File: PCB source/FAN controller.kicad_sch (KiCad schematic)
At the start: 9 parts, among them M1 Fan, Q1 AO3400A

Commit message: Do Cleanup
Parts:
- renumbered C40 to C49, C22 to C50, D1 to D4, Q1 to Q4, R10 to R23, R11 to R24, R13 to R25, R12 to R26
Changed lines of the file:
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@@
 		(dnp no)
 		(fields_autoplaced yes)
-		(property "Reference" "#PWR039"
+		(property "Reference" "#PWR099"
 			(at 100.33 78.74 0)
 			(effects
@@
 			(project ""
 				(path "/3103c9de-f1ba-4d51-8bfc-798df1c75e2f/ddd125ab-d3f0-4627-8bf0-c5c0a9168cb7"
-					(reference "#PWR039")
+					(reference "#PWR099")
 					(unit 1)
 				)
@@
 		(on_board yes)
 		(dnp yes)
-		(property "Reference" "R10"
+		(property "Reference" "R23"
 			(at 114.554 78.486 90)
 			(effects
@@
 			(project ""
 				(path "/3103c9de-f1ba-4d51-8bfc-798df1c75e2f/ddd125ab-d3f0-4627-8bf0-c5c0a9168cb7"
-					(reference "R10")
+					(reference "R23")
 					(unit 1)
 				)
@@
 		(dnp no)
 		(fields_autoplaced yes)
-		(property "Reference" "#PWR038"
+		(property "Reference" "#PWR0100"
 			(at 109.22 78.74 0)
 			(effects
@@
 			(project ""
 				(path "/3103c9de-f1ba-4d51-8bfc-798df1c75e2f/ddd125ab-d3f0-4627-8bf0-c5c0a9168cb7"
-					(reference "#PWR038")
+					(reference "#PWR0100")
 					(unit 1)
 				)
@@
 		(dnp no)
 		(fields_autoplaced yes)
-		(property "Reference" "Q1"
+		(property "Reference" "Q4"
 			(at 175.26 114.3 0)
 			(effects
@@
 			(project ""
 				(path "/3103c9de-f1ba-4d51-8bfc-798df1c75e2f/ddd125ab-d3f0-4627-8bf0-c5c0a9168cb7"
-					(reference "Q1")
+					(reference "Q4")
 					(unit 1)
 				)
@@
 		(dnp no)
 		(fields_autoplaced yes)
-		(property "Reference" "#PWR041"
+		(property "Reference" "#PWR0102"
 			(at 152.4 135.89 0)
 			(effects
@@
 			(project "OrangePie"
 				(path "/3103c9de-f1ba-4d51-8bfc-798df1c75e2f/ddd125ab-d3f0-4627-8bf0-c5c0a9168cb7"
-					(reference "#PWR041")
+					(reference "#PWR0102")
 					(unit 1)
 				)
@@
 		(dnp no)
 		(fields_autoplaced yes)
-		(property "Reference" "R13"
+		(property "Reference" "R25"
 			(at 142.24 111.76 90)
 			(effects
@@
 			(project ""
 				(path "/3103c9de-f1ba-4d51-8bfc-798df1c75e2f/ddd125ab-d3f0-4627-8bf0-c5c0a9168cb7"
-					(reference "R13")
+					(reference "R25")
 					(unit 1)
 				)
@@
 		(dnp no)
 		(fields_autoplaced yes)
-		(property "Reference" "C40"
+		(property "Reference" "C49"
 			(at 157.48 93.98 0)
 			(effects
@@
 			(project "OrangePie"
 				(path "/3103c9de-f1ba-4d51-8bfc-798df1c75e2f/ddd125ab-d3f0-4627-8bf0-c5c0a9168cb7"
-					(reference "C40")
+					(reference "C49")
 					(unit 1)
 				)
@@
 		(dnp no)
 		(fields_autoplaced yes)
-		(property "Reference" "R12"
+		(property "Reference" "R26"
 			(at 154.94 121.92 0)
 			(effects
@@
 			(project ""
 				(path "/3103c9de-f1ba-4d51-8bfc-798df1c75e2f/ddd125ab-d3f0-4627-8bf0-c5c0a9168cb7"
-					(reference "R12")
+					(reference "R26")
 					(unit 1)
 				)
@@
 		(on_board yes)
 		(dnp no)
-		(property "Reference" "C22"
+		(property "Reference" "C50"
 			(at 148.844 96.52 90)
 			(effects
@@
 			(project "OrangePie"
 				(path "/3103c9de-f1ba-4d51-8bfc-798df1c75e2f/ddd125ab-d3f0-4627-8bf0-c5c0a9168cb7"
-					(reference "C22")
+					(reference "C50")
 					(unit 1)
 				)
@@
 		(dnp no)
 		(fields_autoplaced yes)
-		(property "Reference" "D1"
+		(property "Reference" "D4"
 			(at 187.96 94.615 0)
 			(effects
@@
 			(project ""
 				(path "/3103c9de-f1ba-4d51-8bfc-798df1c75e2f/ddd125ab-d3f0-4627-8bf0-c5c0a9168cb7"
-					(reference "D1")
+					(reference "D4")
 					(unit 1)
 				)
@@
 		(dnp no)
 		(fields_autoplaced yes)
-		(property "Reference" "#PWR043"
+		(property "Reference" "#PWR0103"
 			(at 171.45 135.89 0)
 			(effects
@@
 			(project "OrangePie"
 				(path "/3103c9de-f1ba-4d51-8bfc-798df1c75e2f/ddd125ab-d3f0-4627-8bf0-c5c0a9168cb7"
-					(reference "#PWR043")
+					(reference "#PWR0103")
 					(unit 1)
 				)
@@
 		(on_board yes)
 		(dnp no)
-		(property "Reference" "#PWR042"
+		(property "Reference" "#PWR0101"
 			(at 154.94 111.76 0)
 			(effects
@@
 			(project "OrangePie"
 				(path "/3103c9de-f1ba-4d51-8bfc-798df1c75e2f/ddd125ab-d3f0-4627-8bf0-c5c0a9168cb7"
-					(reference "#PWR042")
+					(reference "#PWR0101")
 					(unit 1)
 				)
@@
 		(on_board yes)
 		(dnp no)
-		(property "Reference" "R11"
+		(property "Reference" "R24"
 			(at 114.3 87.122 90)
 			(effects
@@
 			(project "OrangePie"
 				(path "/3103c9de-f1ba-4d51-8bfc-798df1c75e2f/ddd125ab-d3f0-4627-8bf0-c5c0a9168cb7"
-					(reference "R11")
+					(reference "R24")
 					(unit 1)
 				)

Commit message: Pass ERC
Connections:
- net +12V renamed 12V_IN
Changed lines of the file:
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@@
 	(wire
 		(pts
-			(xy 100.33 74.93) (xy 100.33 88.9)
+			(xy 87.63 86.36) (xy 87.63 88.9)
 		)
 		(stroke
@@
 	(wire
 		(pts
+			(xy 102.87 80.01) (xy 115.57 80.01)
+		)
+		(stroke
+			(width 0)
+			(type default)
+		)
+	)
+	(wire
+		(pts
 			(xy 133.35 83.82) (xy 133.35 88.9)
 		)
@@
 	(wire
 		(pts
-			(xy 109.22 80.01) (xy 115.57 80.01)
-		)
-		(stroke
-			(width 0)
-			(type default)
-		)
-	)
-	(wire
-		(pts
 			(xy 154.94 88.9) (xy 148.59 88.9)
 		)
@@
 	(wire
 		(pts
-			(xy 109.22 74.93) (xy 109.22 80.01)
-		)
-		(stroke
-			(width 0)
-			(type default)
-		)
-	)
-	(wire
-		(pts
 			(xy 185.42 83.82) (xy 171.45 83.82)
 		)
@@
 	(wire
 		(pts
-			(xy 100.33 88.9) (xy 115.57 88.9)
+			(xy 87.63 88.9) (xy 115.57 88.9)
 		)
 		(stroke
@@
 			(width 0)
 			(type default)
+		)
+	)
+	(hierarchical_label "12V_IN"
+		(shape input)
+		(at 102.87 80.01 180)
+		(fields_autoplaced yes)
+		(effects
+			(font
+				(size 1.27 1.27)
+			)
+			(justify right)
 		)
 	)
@@
 	(symbol
 		(lib_id "power:+5V")
-		(at 100.33 74.93 0)
+		(at 87.63 86.36 0)
 		(unit 1)
 		(exclude_from_sim no)
@@
 		(fields_autoplaced yes)
 		(property "Reference" "#PWR099"
-			(at 100.33 78.74 0)
+			(at 87.63 90.17 0)
 			(effects
 				(font
@@
 		)
 		(property "Value" "+5V"
-			(at 100.33 69.85 0)
+			(at 87.63 81.28 0)
 			(effects
 				(font
@@
 		)
 		(property "Footprint" ""
-			(at 100.33 74.93 0)
+			(at 87.63 86.36 0)
 			(effects
 				(font
@@
 		)
 		(property "Datasheet" ""
-			(at 100.33 74.93 0)
+			(at 87.63 86.36 0)
 			(effects
 				(font
@@
 		)
 		(property "Description" "Power symbol creates a global label with name \"+5V\""
-			(at 100.33 74.93 0)
+			(at 87.63 86.36 0)
 			(effects
 				(font
@@
 					(unit 1)
 				)
-			)
-		)
-	)
-	(symbol
-		(lib_id "power:+12V")
-		(at 109.22 74.93 0)
-		(unit 1)
-		(exclude_from_sim no)
-		(in_bom yes)
-		(on_board yes)
-		(dnp no)
-		(fields_autoplaced yes)
-		(property "Reference" "#PWR0100"
-			(at 109.22 78.74 0)
-			(effects
-				(font
-					(size 1.27 1.27)
-				)
-				(hide yes)
-			)
-		)
-		(property "Value" "+12V"
-			(at 109.22 69.85 0)
-			(effects
-				(font
-					(size 1.27 1.27)
-				)
-			)
-		)
-		(property "Footprint" ""
-			(at 109.22 74.93 0)
-			(effects
-				(font
-					(size 1.27 1.27)
-				)
-				(hide yes)
-			)
-		)
-		(property "Datasheet" ""
-			(at 109.22 74.93 0)
-			(effects
-				(font
-					(size 1.27 1.27)
-				)
-				(hide yes)
-			)
-		)
-		(property "Description" "Power symbol creates a global label with name \"+12V\""
-			(at 109.22 74.93 0)
-			(effects
-				(font
-					(size 1.27 1.27)
-				)
-				(hide yes)
-			)
-		)
-		(pin "1"
-		)
-		(instances
-			(project ""
-				(path "/3103c9de-f1ba-4d51-8bfc-798df1c75e2f/ddd125ab-d3f0-4627-8bf0-c5c0a9168cb7"
-					(reference "#PWR0100")
-					(unit 1)
-				)

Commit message: Fix schematic
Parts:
- removed Q4: AO3400A, Package_TO_SOT_SMD:SOT-23, symbol Transistor_FET:AO3400A
- added Q4: AO3400A, PCM_JLCPCB:Q_SOT-23, symbol PCM_JLCPCB-Transistors:NMOS,AO3400A
- C49: Price 0.031USD -> 0.035USD; Stock 4852625 -> 821695
- D4: Stock 26897 -> 26535
- R23, R24: Stock 5514860 -> 6249348
- R25: Stock 778464 -> 1074828
- R26: Stock 6666349 -> 13746052
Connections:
- net GND: now also Q4.2 (S)
- net at R25.2, R26.2: now also Q4.1 (G)
- net at D4.2, M1.2 (-): now also Q4.3 (D)
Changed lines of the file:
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@@
 (kicad_sch
-	(version 20231120)
+	(version 20250114)
 	(generator "eeschema")
-	(generator_version "8.0")
+	(generator_version "9.0")
 	(paper "A4")
 	(title_block
@@
 		(shape input)
 		(at 102.87 80.01 180)
-		(fields_autoplaced yes)
 		(effects
 			(font
@@
 		(shape input)
 		(at 121.92 115.57 180)
-		(fields_autoplaced yes)
 		(effects
 			(font
@@
 			)
 		)
-		(property "Stock" "5514860"
+		(property "Stock" "6249348"
 			(at 119.38 80.01 0)
 			(effects
@@
 				(path "/3103c9de-f1ba-4d51-8bfc-798df1c75e2f/ddd125ab-d3f0-4627-8bf0-c5c0a9168cb7"
 					(reference "R23")
-					(unit 1)
-				)
-			)
-		)
-	)
-	(symbol
-		(lib_id "Transistor_FET:AO3400A")
-		(at 168.91 115.57 0)
-		(unit 1)
-		(exclude_from_sim no)
-		(in_bom yes)
-		(on_board yes)
-		(dnp no)
-		(fields_autoplaced yes)
-		(property "Reference" "Q4"
-			(at 175.26 114.3 0)
-			(effects
-				(font
-					(size 1.27 1.27)
-				)
-				(justify left)
-			)
-		)
-		(property "Value" "AO3400A"
-			(at 175.26 116.84 0)
-			(effects
-				(font
-					(size 1.27 1.27)
-				)
-				(justify left)
-			)
-		)
-		(property "Footprint" "Package_TO_SOT_SMD:SOT-23"
-			(at 173.99 117.475 0)
-			(effects
-				(font
-					(size 1.27 1.27)
-					(italic yes)
-				)
-				(justify left)
-				(hide yes)
-			)
-		)
-		(property "Datasheet" "http://www.aosmd.com/pdfs/datasheet/AO3400A.pdf"
-			(at 173.99 119.38 0)
-			(effects
-				(font
-					(size 1.27 1.27)
-				)
-				(justify left)
-				(hide yes)
-			)
-		)
-		(property "Description" "30V Vds, 5.7A Id, N-Channel MOSFET, SOT-23"
-			(at 168.91 115.57 0)
-			(effects
-				(font
-					(size 1.27 1.27)
-				)
-				(hide yes)
-			)
-		)
-		(pin "2"
-		)
-		(pin "1"
-		)
-		(pin "3"
-		)
-		(instances
-			(project ""
-				(path "/3103c9de-f1ba-4d51-8bfc-798df1c75e2f/ddd125ab-d3f0-4627-8bf0-c5c0a9168cb7"
-					(reference "Q4")
 					(unit 1)
 				)
@@
 			)
 		)
-		(property "Stock" "778464"
+		(property "Stock" "1074828"
 			(at 142.24 115.57 0)
 			(effects
@@
 			)
 		)
-		(property "Stock" "4852625"
+		(property "Stock" "821695"
 			(at 154.94 95.25 0)
 			(effects
@@
 			)
 		)
-		(property "Price" "0.031USD"
+		(property "Price" "0.035USD"
 			(at 154.94 95.25 0)
 			(effects
@@
 			)
 		)
-		(property "Stock" "6666349"
+		(property "Stock" "13746052"
 			(at 152.4 121.92 0)
 			(effects
@@
 			)
 		)
-		(property "Stock" "26897"
+		(property "Stock" "26535"
 			(at 185.42 95.25 0)
 			(effects
@@
 			)
 		)
-		(property "Stock" "5514860"
+		(property "Stock" "6249348"
 			(at 119.38 88.9 0)
 			(effects
@@
 					(unit 1)
 				)
+			)
+		)
+	)
+	(symbol
+		(lib_id "PCM_JLCPCB-Transistors:NMOS,AO3400A")
+		(at 168.91 115.57 0)
+		(unit 1)
+		(exclude_from_sim no)
+		(in_bom yes)
+		(on_board yes)
+		(dnp no)
+		(fields_autoplaced yes)
+		(property "Reference" "Q4"
+			(at 175.26 114.2999 0)
+			(effects
+				(font
+					(size 1.27 1.27)
+				)
+				(justify left)
+			)
+		)
+		(property "Value" "AO3400A"
+			(at 175.26 116.84 0)
+			(effects
+				(font
+					(size 0.8 0.8)
+				)
+				(justify left)
+			)
+		)
+		(property "Footprint" "PCM_JLCPCB:Q_SOT-23"
+			(at 167.132 115.57 90)
+			(effects
+				(font
+					(size 1.27 1.27)
+				)
+				(hide yes)
+			)
+		)
+		(property "Datasheet" "https://www.lcsc.com/datasheet/lcsc_datasheet_1811081213_Alpha---Omega-Semicon-AO3400A_C20917.pdf"
+			(at 168.91 115.57 0)
+			(effects
+				(font
+					(size 1.27 1.27)
+				)
+				(hide yes)
+			)
+		)
+		(property "Description" "30V 5.7A 26.5mΩ@10V,5.7A 1.4W 1.5V@250uA 1 N-Channel SOT-23-3L MOSFETs ROHS"
+			(at 168.91 115.57 0)
+			(effects
+				(font
+					(size 1.27 1.27)
+				)
+				(hide yes)
+			)
+		)
+		(property "LCSC" "C20917"
+			(at 168.91 115.57 0)
+			(effects
+				(font
+					(size 1.27 1.27)
+				)
+				(hide yes)
+			)
+		)
+		(property "Stock" "670221"
+			(at 168.91 115.57 0)
+			(effects
+				(font
+					(size 1.27 1.27)
+				)
+				(hide yes)
+			)
+		)
+		(property "Price" "0.088USD"
+			(at 168.91 115.57 0)
+			(effects
+				(font
+					(size 1.27 1.27)
+				)
+				(hide yes)
+			)
+		)
+		(property "Process" "SMT"
+			(at 168.91 115.57 0)
+			(effects
+				(font
+					(size 1.27 1.27)
+				)
+				(hide yes)
+			)
+		)
+		(property "Minimum Qty" "5"
+			(at 168.91 115.57 0)
+			(effects
+				(font
+					(size 1.27 1.27)
+				)
+				(hide yes)
+			)
+		)
+		(property "Attrition Qty" "4"
+			(at 168.91 115.57 0)
+			(effects
+				(font
+					(size 1.27 1.27)
+				)
+				(hide yes)
+			)
+		)
+		(property "Class" "Basic Component"
+			(at 168.91 115.57 0)
+			(effects
+				(font
+					(size 1.27 1.27)
+				)
+				(hide yes)
+			)
+		)
+		(property "Category" "Transistors,MOSFETs"
+			(at 168.91 115.57 0)
+			(effects
+				(font
+					(size 1.27 1.27)
+				)
+				(hide yes)
+			)
+		)
+		(property "Manufacturer" "Alpha & Omega Semicon"
+			(at 168.91 115.57 0)
+			(effects
+				(font
+					(size 1.27 1.27)
+				)
+				(hide yes)
+			)
+		)
+		(property "Part" "AO3400A"
+			(at 168.91 115.57 0)
+			(effects
+				(font
+					(size 1.27 1.27)
+				)
+				(hide yes)
+			)
+		)
+		(property "Continuous Drain Current (Id)" "5.7A"
+			(at 168.91 115.57 0)
+			(effects
+				(font
+					(size 1.27 1.27)
+				)
+				(hide yes)
+			)
+		)
+		(property "Input Capacitance (Ciss@Vds)" "630pF@15V"
+			(at 168.91 115.57 0)
+			(effects
+				(font
+					(size 1.27 1.27)
+				)
+				(hide yes)
+			)
+		)
+		(property "Operating Temperature" "-55°C~+150°C@(Tj)"
+			(at 168.91 115.57 0)
+			(effects
+				(font
+					(size 1.27 1.27)
+				)
+				(hide yes)
+			)
+		)
+		(property "Type" "1 N-channel"
+			(at 168.91 115.57 0)
+			(effects
+				(font
+					(size 1.27 1.27)
+				)
+				(hide yes)
+			)
+		)
+		(property "Drain Source Voltage (Vdss)" "30V"
+			(at 168.91 115.57 0)
+			(effects
+				(font
+					(size 1.27 1.27)
+				)
+				(hide yes)
+			)
+		)
+		(property "Power Dissipation (Pd)" "1.4W"
+			(at 168.91 115.57 0)
+			(effects
+				(font
+					(size 1.27 1.27)
+				)
+				(hide yes)
+			)
+		)
+		(property "Gate Threshold Voltage (Vgs(th)@Id)" "1.5V@250uA"
+			(at 168.91 115.57 0)
+			(effects
+				(font
+					(size 1.27 1.27)
+				)
+				(hide yes)
+			)
+		)
+		(property "Drain Source On Resistance (RDS(on)@Vgs,Id)" "26.5mΩ@10V,5.7A"
+			(at 168.91 115.57 0)
+			(effects
+				(font
+					(size 1.27 1.27)
+				)
+				(hide yes)
+			)
+		)
+		(property "Total Gate Charge (Qg@Vgs)" "7nC@4.5V"
+			(at 168.91 115.57 0)
+			(effects
+				(font
+					(size 1.27 1.27)
+				)
+				(hide yes)
+			)
+		)
+		(pin "1"
+		)
+		(pin "3"
+		)
+		(pin "2"
+		)
+		(instances
+			(project ""
+				(path "/3103c9de-f1ba-4d51-8bfc-798df1c75e2f/ddd125ab-d3f0-4627-8bf0-c5c0a9168cb7"
+					(reference "Q4")
+					(unit 1)
+				)

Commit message: [3] Start layout
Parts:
- removed C50: 47uF, Capacitor_SMD:CP_Elec_6.3x5.4, symbol Device:C_Polarized
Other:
- moved on the sheet: C49
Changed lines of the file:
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@@
-	)
-	(junction
-		(at 154.94 102.87)
-		(diameter 0)
-		(color 0 0 0 0)
 	)
 	(junction
@@
 		(color 0 0 0 0)
 	)
-	(junction
-		(at 148.59 88.9)
-		(diameter 0)
-		(color 0 0 0 0)
-	)
 	(wire
 		(pts
@@
 	(wire
 		(pts
-			(xy 148.59 88.9) (xy 142.24 88.9)
-		)
-		(stroke
-			(width 0)
-			(type default)
-		)
-	)
-	(wire
-		(pts
 			(xy 133.35 83.82) (xy 148.59 83.82)
 		)
@@
 	(wire
 		(pts
-			(xy 148.59 83.82) (xy 148.59 88.9)
+			(xy 148.59 83.82) (xy 148.59 91.44)
 		)
 		(stroke
@@
 	(wire
 		(pts
-			(xy 154.94 102.87) (xy 154.94 105.41)
+			(xy 148.59 99.06) (xy 148.59 105.41)
 		)
 		(stroke
@@
 	(wire
 		(pts
-			(xy 154.94 99.06) (xy 154.94 102.87)
-		)
-		(stroke
-			(width 0)
-			(type default)
-		)
-	)
-	(wire
-		(pts
-			(xy 142.24 102.87) (xy 154.94 102.87)
-		)
-		(stroke
-			(width 0)
-			(type default)
-		)
-	)
-	(wire
-		(pts
-			(xy 154.94 88.9) (xy 148.59 88.9)
-		)
-		(stroke
-			(width 0)
-			(type default)
-		)
-	)
-	(wire
-		(pts
 			(xy 185.42 83.82) (xy 171.45 83.82)
 		)
@@
 	(wire
 		(pts
-			(xy 154.94 88.9) (xy 154.94 91.44)
-		)
-		(stroke
-			(width 0)
-			(type default)
-		)
-	)
-	(wire
-		(pts
 			(xy 171.45 101.6) (xy 171.45 106.68)
 		)
@@
 	(wire
 		(pts
-			(xy 142.24 102.87) (xy 142.24 100.33)
-		)
-		(stroke
-			(width 0)
-			(type default)
-		)
-	)
-	(wire
-		(pts
 			(xy 87.63 88.9) (xy 115.57 88.9)
 		)
@@
 		(pts
 			(xy 185.42 106.68) (xy 171.45 106.68)
-		)
-		(stroke
-			(width 0)
-			(type default)
-		)
-	)
-	(wire
-		(pts
-			(xy 142.24 88.9) (xy 142.24 92.71)
 		)
 		(stroke
@@
 	(symbol
 		(lib_id "PCM_JLCPCB-Capacitors:1206,10uF")
-		(at 154.94 95.25 0)
+		(at 148.59 95.25 0)
 		(unit 1)
 		(exclude_from_sim no)
@@
 		(fields_autoplaced yes)
 		(property "Reference" "C49"
-			(at 157.48 93.98 0)
+			(at 151.13 93.98 0)
 			(effects
 				(font
@@
 		)
 		(property "Value" "10uF"
-			(at 157.48 95.885 0)
+			(at 151.13 95.885 0)
 			(effects
 				(font
@@
 		)
 		(property "Footprint" "PCM_JLCPCB:C_1206"
-			(at 153.162 95.25 90)
+			(at 146.812 95.25 90)
 			(effects
 				(font
@@
 		)
 		(property "Datasheet" "https://www.lcsc.com/datasheet/lcsc_datasheet_2304140030_Samsung-Electro-Mechanics-CL31A106KBHNNNE_C13585.pdf"
-			(at 154.94 95.25 0)
+			(at 148.59 95.25 0)
 			(effects
 				(font
@@
 		)
 		(property "Description" "50V 10uF X5R ±10% 1206 Multilayer Ceramic Capacitors MLCC - SMD/SMT ROHS"
-			(at 154.94 95.25 0)
+			(at 148.59 95.25 0)
 			(effects
 				(font
@@
 		)
 		(property "LCSC" "C13585"
-			(at 154.94 95.25 0)
+			(at 148.59 95.25 0)
 			(effects
 				(font
@@
 		)
 		(property "Stock" "821695"
-			(at 154.94 95.25 0)
+			(at 148.59 95.25 0)
 			(effects
 				(font
@@
 		)
 		(property "Price" "0.035USD"
-			(at 154.94 95.25 0)
+			(at 148.59 95.25 0)
 			(effects
 				(font
@@
 		)
 		(property "Process" "SMT"
-			(at 154.94 95.25 0)
+			(at 148.59 95.25 0)
 			(effects
 				(font
@@
 		)
 		(property "Minimum Qty" "5"
-			(at 154.94 95.25 0)
+			(at 148.59 95.25 0)
 			(effects
 				(font
@@
 		)
 		(property "Attrition Qty" "4"
-			(at 154.94 95.25 0)
+			(at 148.59 95.25 0)
 			(effects
 				(font
@@
 		)
 		(property "Class" "Basic Component"
-			(at 154.94 95.25 0)
+			(at 148.59 95.25 0)
 			(effects
 				(font
@@
 		)
 		(property "Category" "Capacitors,Multilayer Ceramic Capacitors MLCC - SMD/SMT"
-			(at 154.94 95.25 0)
+			(at 148.59 95.25 0)
 			(effects
 				(font
@@
 		)
 		(property "Manufacturer" "Samsung Electro-Mechanics"
-			(at 154.94 95.25 0)
+			(at 148.59 95.25 0)
 			(effects
 				(font
@@
 		)
 		(property "Part" "CL31A106KBHNNNE"
-			(at 154.94 95.25 0)
+			(at 148.59 95.25 0)
 			(effects
 				(font
@@
 		)
 		(property "Voltage Rated" "50V"
-			(at 157.48 97.155 0)
+			(at 151.13 97.155 0)
 			(effects
 				(font
@@
 		)
 		(property "Tolerance" "±10%"
-			(at 154.94 95.25 0)
+			(at 148.59 95.25 0)
 			(effects
 				(font
@@
 		)
 		(property "Capacitance" "10uF"
-			(at 154.94 95.25 0)
+			(at 148.59 95.25 0)
 			(effects
 				(font
@@
 		)
 		(property "Temperature Coefficient" "X5R"
-			(at 154.94 95.25 0)
+			(at 148.59 95.25 0)
 			(effects
 				(font
@@
 	)
 	(symbol
-		(lib_id "Device:C_Polarized")
-		(at 142.24 96.52 0)
-		(unit 1)
-		(exclude_from_sim no)
-		(in_bom yes)
-		(on_board yes)
-		(dnp no)
-		(property "Reference" "C50"
-			(at 148.844 96.52 90)
-			(effects
-				(font
-					(size 1.27 1.27)
-				)
-			)
-		)
-		(property "Value" "47uF"
-			(at 146.304 96.52 90)
-			(effects
-				(font
-					(size 1.27 1.27)
-				)
-			)
-		)
-		(property "Footprint" "Capacitor_SMD:CP_Elec_6.3x5.4"
-			(at 143.2052 100.33 0)
-			(effects
-				(font
-					(size 1.27 1.27)
-				)
-				(hide yes)
-			)
-		)
-		(property "Datasheet" "~"
-			(at 142.24 96.52 0)
-			(effects
-				(font
-					(size 1.27 1.27)
-				)
-				(hide yes)
-			)
-		)
-		(property "Description" "Polarized capacitor"
-			(at 142.24 96.52 0)
-			(effects
-				(font
-					(size 1.27 1.27)
-				)
-				(hide yes)
-			)
-		)
-		(property "LCSC" " C90276"
-			(at 142.24 96.52 90)
-			(effects
-				(font
-					(size 1.27 1.27)
-				)
-				(hide yes)
-			)
-		)
-		(property "MPN" "VT1V470M0605"
-			(at 142.24 96.52 90)
-			(effects
-				(font
-					(size 1.27 1.27)
-				)
-				(hide yes)
-			)
-		)
-		(pin "1"
-		)
-		(pin "2"
-		)
-		(instances
-			(project "OrangePie"
-				(path "/3103c9de-f1ba-4d51-8bfc-798df1c75e2f/ddd125ab-d3f0-4627-8bf0-c5c0a9168cb7"
-					(reference "C50")
-					(unit 1)
-				)
-			)
-		)
-	)
-	(symbol
 		(lib_id "Motor:Fan")
 		(at 171.45 96.52 0)
@@
 	(symbol
 		(lib_id "power:GND")
-		(at 154.94 105.41 0)
+		(at 148.59 105.41 0)
 		(unit 1)
 		(exclude_from_sim no)
@@
 		(dnp no)
 		(property "Reference" "#PWR0101"
-			(at 154.94 111.76 0)
+			(at 148.59 111.76 0)
 			(effects
 				(font
@@
 		)
 		(property "Value" "GND"
-			(at 159.258 107.188 0)
+			(at 152.908 107.188 0)
 			(effects
 				(font
@@
 		)
 		(property "Footprint" ""
-			(at 154.94 105.41 0)
+			(at 148.59 105.41 0)
 			(effects
 				(font
@@
 		)
 		(property "Datasheet" ""
-			(at 154.94 105.41 0)
+			(at 148.59 105.41 0)
 			(effects
 				(font
@@
 		)
 		(property "Description" "Power symbol creates a global label with name \"GND\" , ground"
-			(at 154.94 105.41 0)
-			(effects
-				(font
+			(at 148.59 105.41 0)
+			(effects
+				(font

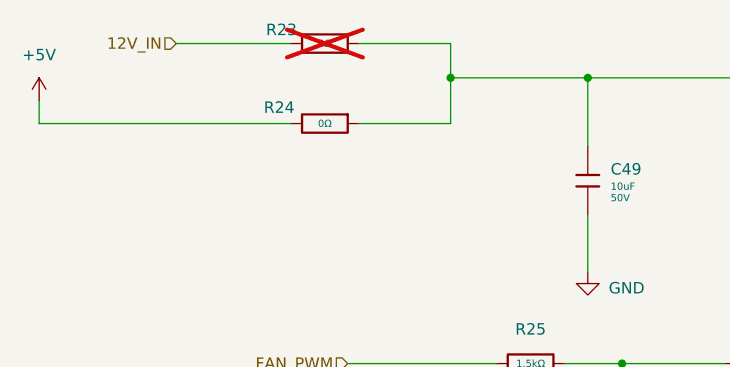
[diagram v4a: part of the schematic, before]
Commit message: Fix can power delivery , fixed placment of the mosfets, CAN power  pull down to avoid DFU boot, added new porgraming connector
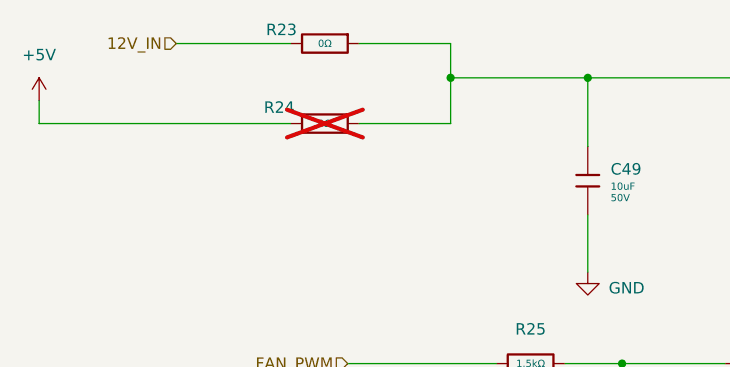
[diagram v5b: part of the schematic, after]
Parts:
- R23: now fitted
- R24: now not fitted
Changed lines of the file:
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@@
 		(in_bom yes)
 		(on_board yes)
-		(dnp yes)
+		(dnp no)
 		(property "Reference" "R23"
 			(at 114.554 78.486 90)
@@
 		(in_bom yes)
 		(on_board yes)
-		(dnp no)
+		(dnp yes)
 		(property "Reference" "R24"
 			(at 114.3 87.122 90)
